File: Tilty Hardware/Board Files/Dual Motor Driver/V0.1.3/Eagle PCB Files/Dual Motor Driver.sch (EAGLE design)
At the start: 42 parts, among them J1 AVR_SPI_PRG_62X3_LOCK, Q1 16MHz, U1 ATMEGA328P, U2 L298_BRIDGE_DRIVER, U3 LM2931

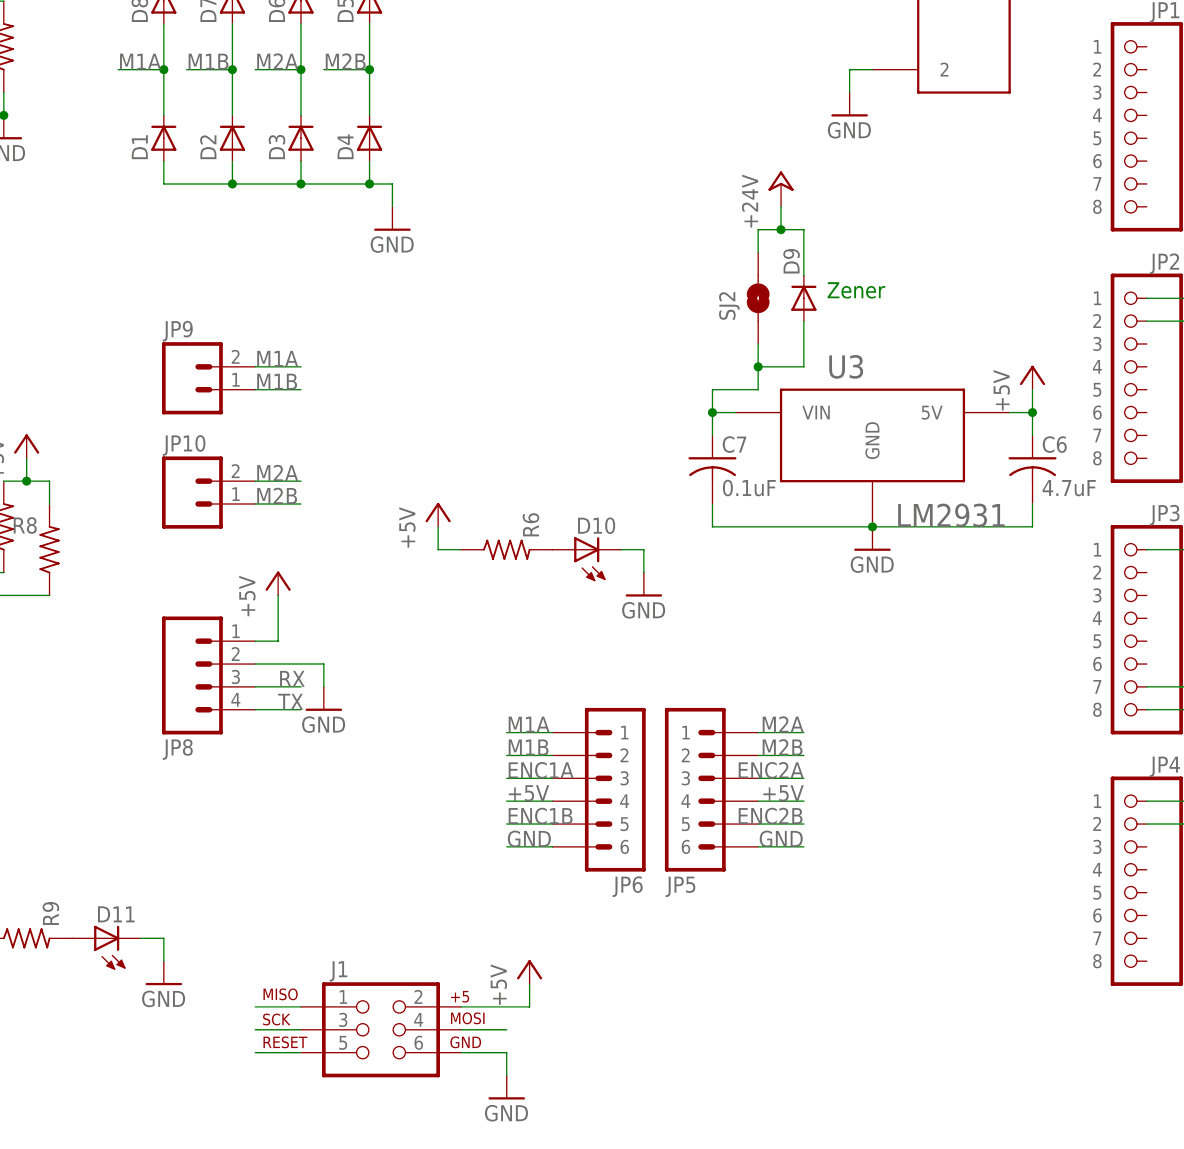
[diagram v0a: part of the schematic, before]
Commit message: Connector changes to dual motor driver
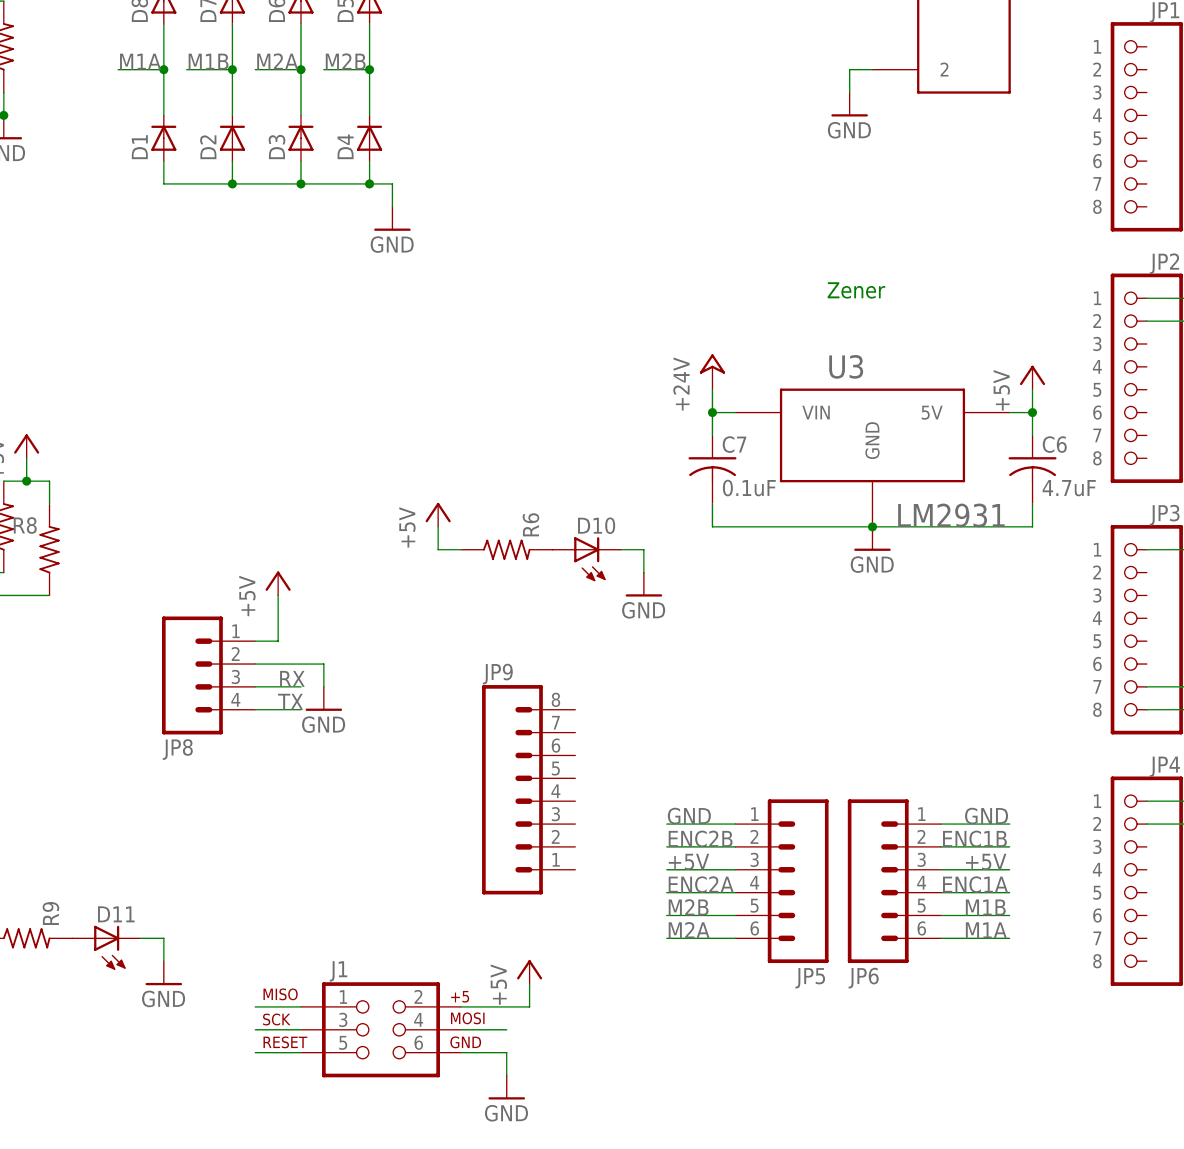
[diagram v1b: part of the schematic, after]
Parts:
- removed D9: (no value), diode:DIODE-DO214AA
- removed JP10: (no value), SparkFun-Connectors:M02PTH
- removed SJ2: SOLDERJUMPERTRACE, SparkFun-Passives:SOLDERJUMPERTRACE
- JP5: value 6PIN-SH_RIGHT_ANGLE -> 6-PIN-CONNECTORLEFT-MOTOR-JST; device con-jst:6PIN-SH_RIGHT_ANGLE -> My Parts:6-PIN-CONNECTORLEFT-MOTOR-JST; PART# SM06B-SRSS-TB(LF)(SN) -> (none)
- JP6: value 6PIN-SH_RIGHT_ANGLE -> 6-PIN-CONNECTORRIGHT-MOTOR-JST; device con-jst:6PIN-SH_RIGHT_ANGLE -> My Parts:6-PIN-CONNECTORRIGHT-MOTOR-JST; PART# SM06B-SRSS-TB(LF)(SN) -> (none)
- JP9: device SparkFun-Connectors:M02PTH -> SparkFun-Connectors:M081X08
- SJ1: value SOLDERJUMPERNC -> SOLDERJUMPERTRACE; device SparkFun-Passives:SOLDERJUMPERNC -> SparkFun-Passives:SOLDERJUMPERTRACE
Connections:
- removed net N$3: C7.1, D9.A, SJ2.1, U3.VIN
- net +24V: now also C7.1, U3.VIN; no longer D9.C, SJ2.2
- net +5V: now also JP5.3, JP6.3; no longer JP5.4, JP6.4
- net ENC1A: now also JP6.4; no longer JP6.3
- net ENC1B: now also JP6.2; no longer JP6.5
- net ENC2A: now also JP5.4; no longer JP5.3
- net ENC2B: now also JP5.2; no longer JP5.5
- net GND: now also JP5.1, JP6.1; no longer JP5.6, JP6.6
- net M1A: now also JP6.6; no longer JP6.1, JP9.2
- net M1B: now also JP6.5; no longer JP6.2, JP9.1
- net M2A: now also JP5.6; no longer JP10.2, JP5.1
- net M2B: now also JP5.5; no longer JP10.1, JP5.2

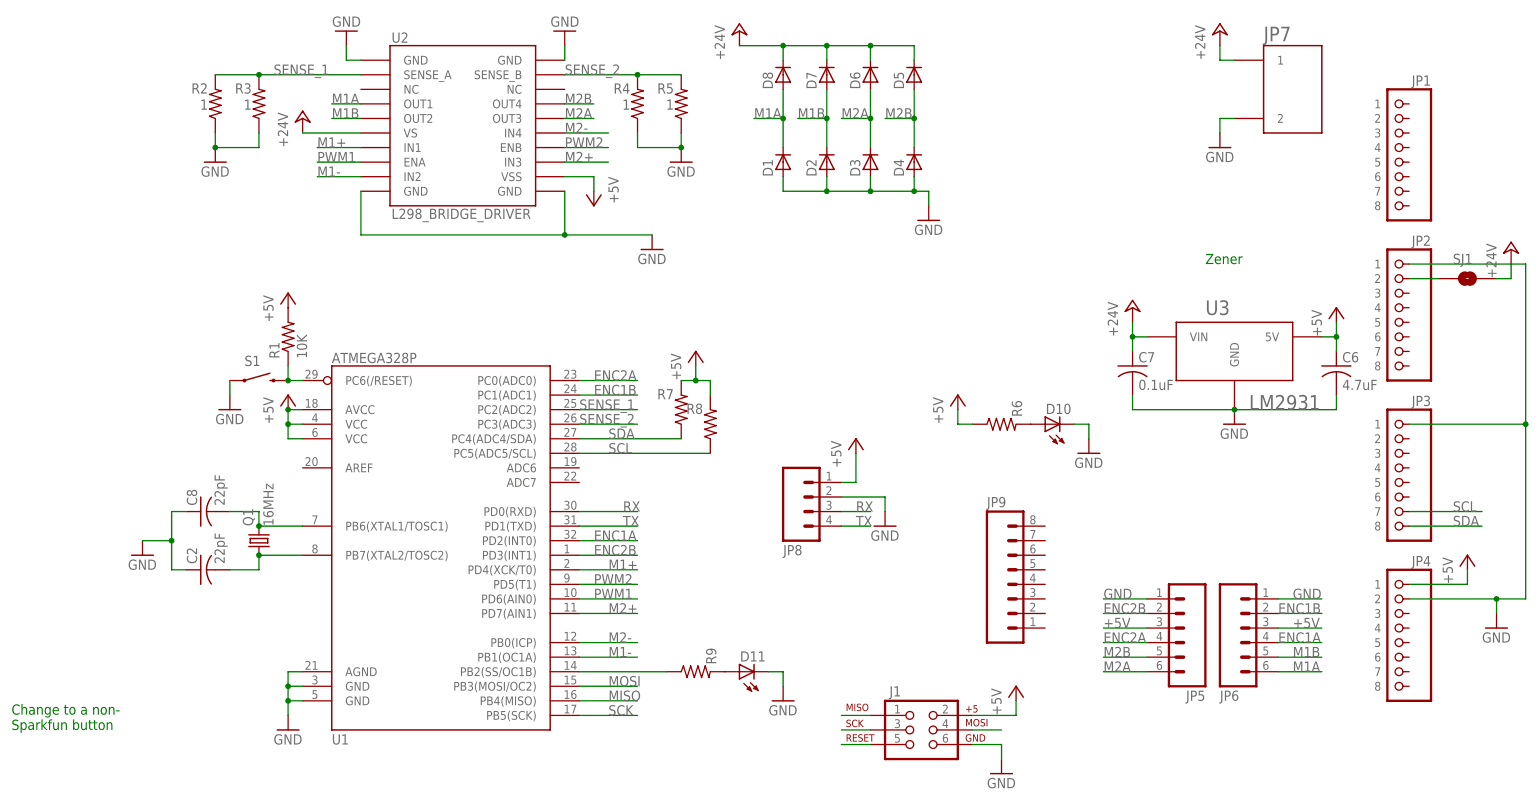
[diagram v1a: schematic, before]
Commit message: Removed redundant Motor Driver backups, changed power connector, and added reverse polarity diode
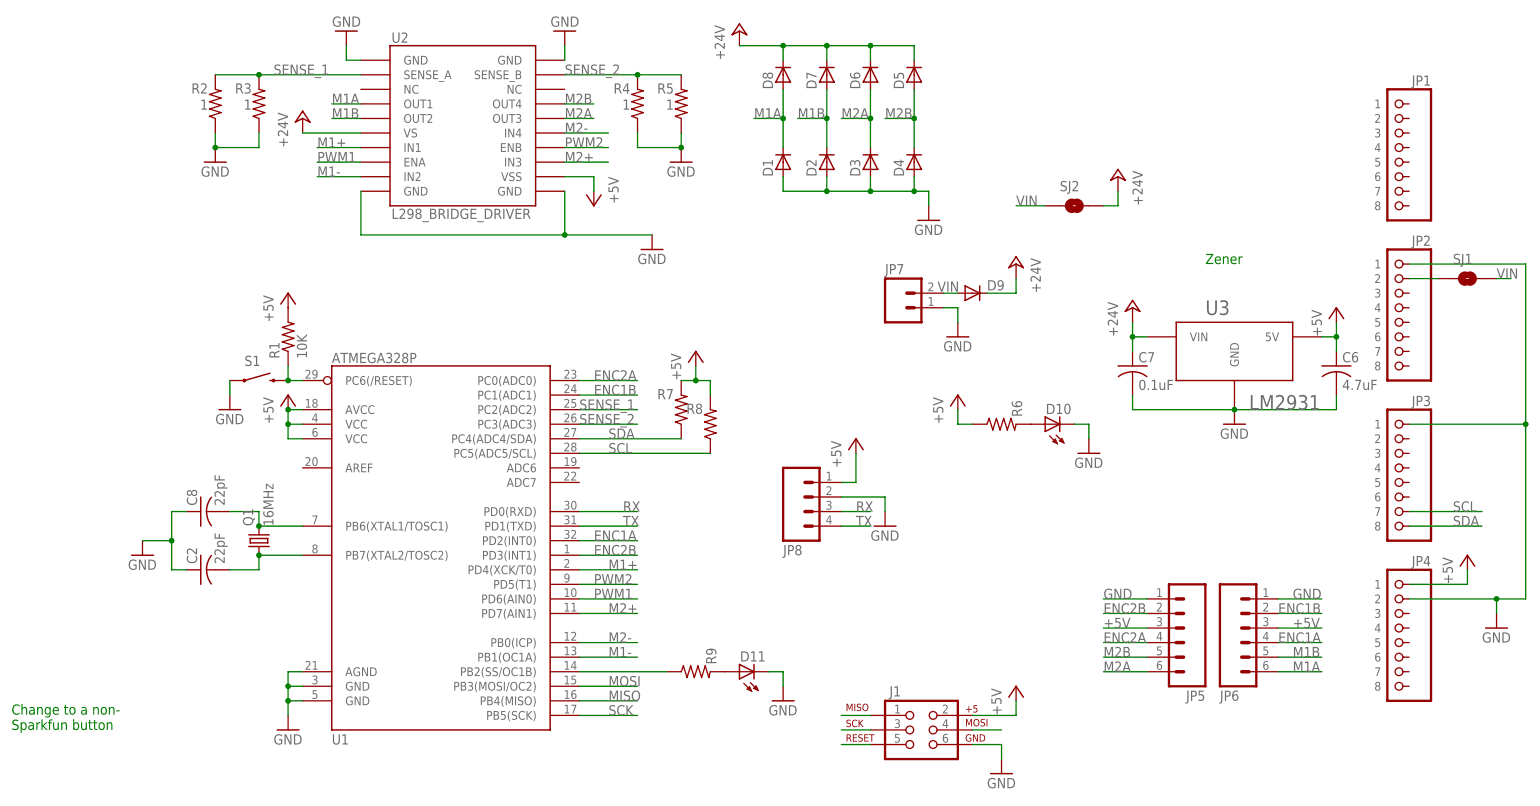
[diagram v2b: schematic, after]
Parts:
- removed JP9: (no value), SparkFun-Connectors:M081X08
- added D9: (no value), SparkFun-DiscreteSemi:DIODESMB
- added SJ2: SOLDERJUMPERNO, SparkFun-Passives:SOLDERJUMPERNO
- JP7: value 2-POS_SMD_TERM_BLOCK -> (none); device My Parts:2-POS_SMD_TERM_BLOCK -> SparkFun-Connectors:M02PTH
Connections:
- new net VIN: D9.A, JP7.2, SJ1.2, SJ2.1
- net +24V: now also D9.C, SJ2.2; no longer JP7.1, SJ1.2
- net GND: now also JP7.1; no longer JP7.2

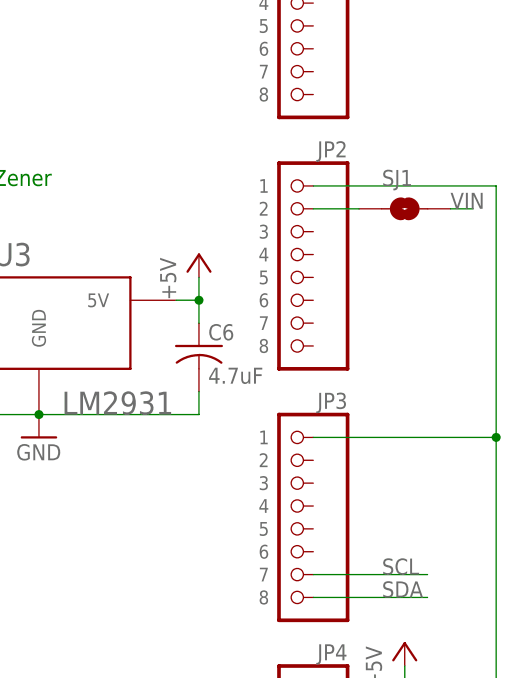
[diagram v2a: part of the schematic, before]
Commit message: Accidental changes (cause Eagle loaded the wrong file) to a version that's out of date anyway, ignore this
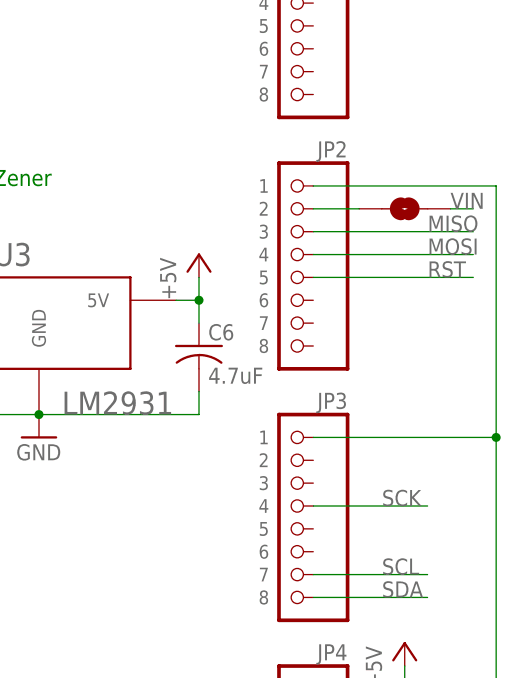
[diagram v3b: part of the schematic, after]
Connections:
- new net RST: JP2.5
- net MISO: now also JP2.3
- net MOSI: now also JP2.4
- net SCK: now also JP3.4
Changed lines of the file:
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@@
 <instance part="C7" gate="G$1" x="198.12" y="68.58"/>
 <instance part="GND11" gate="1" x="60.96" y="127" rot="R180"/>
-<instance part="SJ1" gate="1" x="256.54" y="83.82" smashed="yes">
-<attribute name="NAME" x="254" y="86.36" size="1.778" layer="95"/>
-</instance>
+<instance part="SJ1" gate="1" x="256.54" y="83.82" smashed="yes"/>
 <instance part="Q1" gate="G$1" x="45.72" y="38.1" rot="R90">
 <attribute name="PART#" x="45.72" y="38.1" size="1.778" layer="96" rot="R90" display="off"/>
@@
 <label x="106.68" y="7.62" size="1.778" layer="95"/>
 </segment>
+<segment>
+<pinref part="JP3" gate="G$1" pin="4"/>
+<wire x1="246.38" y1="50.8" x2="259.08" y2="50.8" width="0.1524" layer="91"/>
+<label x="254" y="50.8" size="1.778" layer="95"/>
+</segment>
 </net>
 <net name="MOSI" class="0">
@@
 <label x="106.68" y="12.7" size="1.778" layer="95"/>
 </segment>
+<segment>
+<pinref part="JP2" gate="G$1" pin="4"/>
+<wire x1="246.38" y1="78.74" x2="264.16" y2="78.74" width="0.1524" layer="91"/>
+<label x="259.08" y="78.74" size="1.778" layer="95"/>
+</segment>
 </net>
 <net name="MISO" class="0">
@@
 <wire x1="101.6" y1="10.16" x2="111.76" y2="10.16" width="0.1524" layer="91"/>
 <label x="106.68" y="10.16" size="1.778" layer="95"/>
+</segment>
+<segment>
+<pinref part="JP2" gate="G$1" pin="3"/>
+<wire x1="246.38" y1="81.28" x2="264.16" y2="81.28" width="0.1524" layer="91"/>
+<label x="259.08" y="81.28" size="1.778" layer="95"/>
 </segment>
 </net>
@@
 </segment>
 </net>
+<net name="RST" class="0">
+<segment>
+<pinref part="JP2" gate="G$1" pin="5"/>
+<wire x1="246.38" y1="76.2" x2="264.16" y2="76.2" width="0.1524" layer="91"/>
+<label x="259.08" y="76.2" size="1.778" layer="95"/>
+</segment>
+</net>
